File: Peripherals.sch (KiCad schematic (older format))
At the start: 64 parts, among them J10 Conn_01x01, J11 Conn_01x01, J12 Conn_01x01, J13 Conn_01x04, J14 RCAJack, J5 Conn_01x10, J6 Conn_01x10, J7 Conn_01x10, J8 Conn_01x08, J9 Conn_01x01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

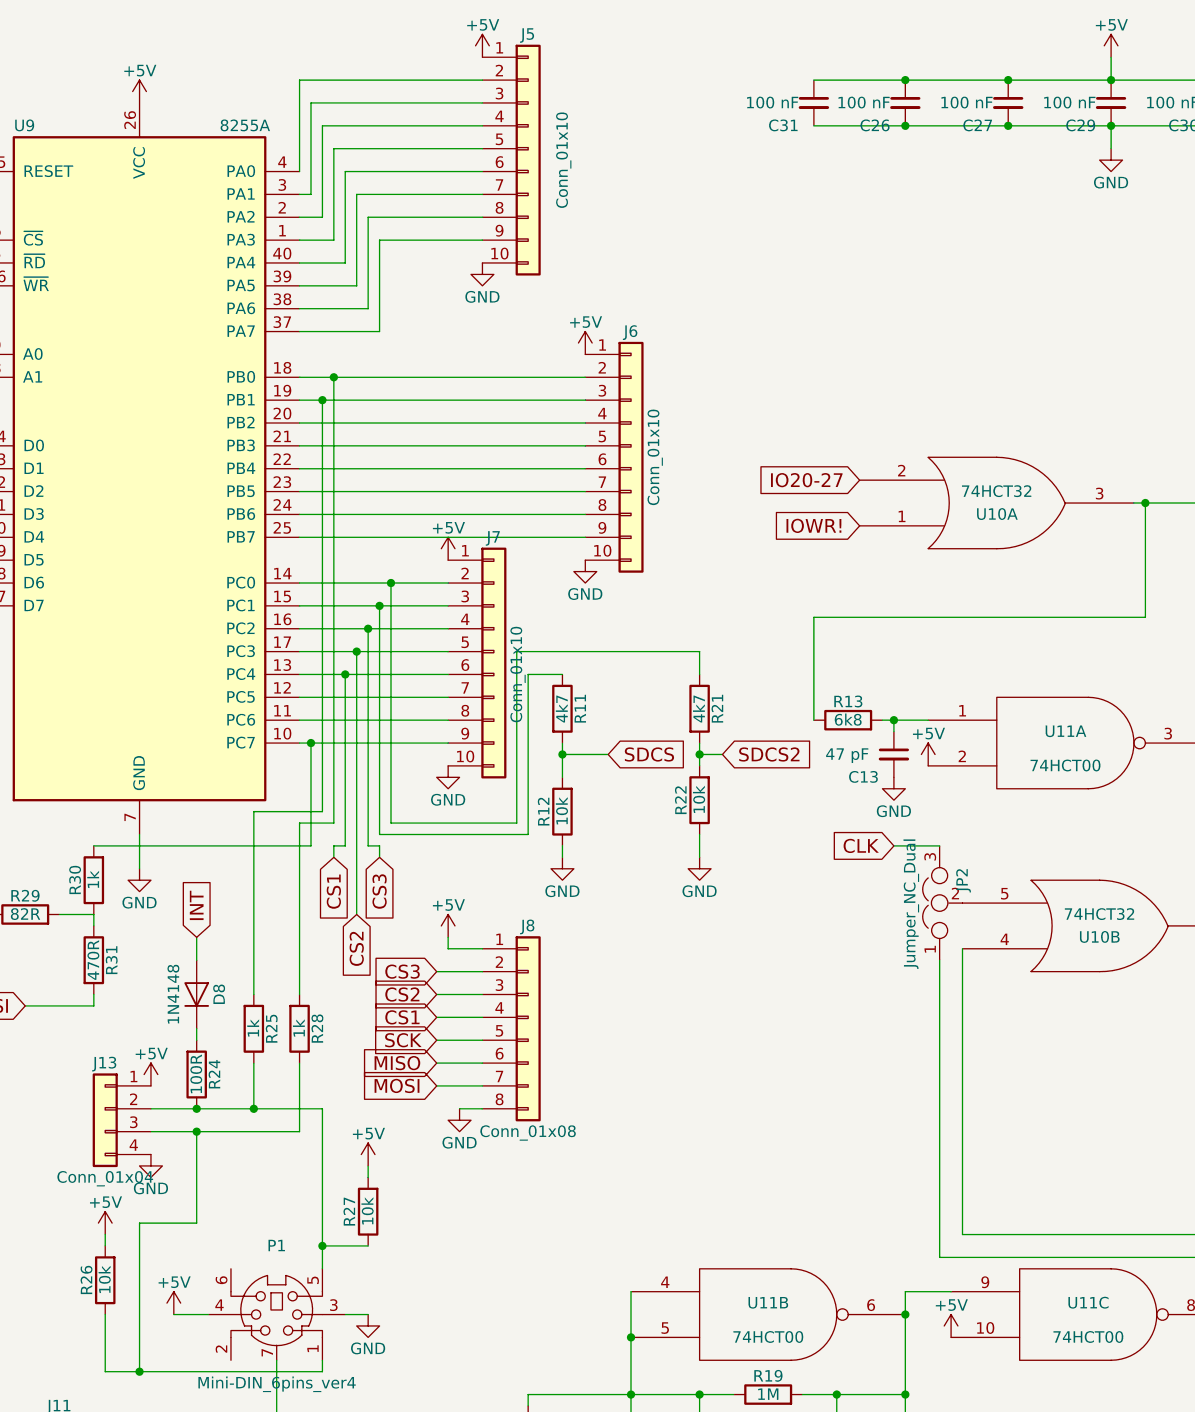
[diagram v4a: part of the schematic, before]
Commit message: Fixed PS/2 interrupt line
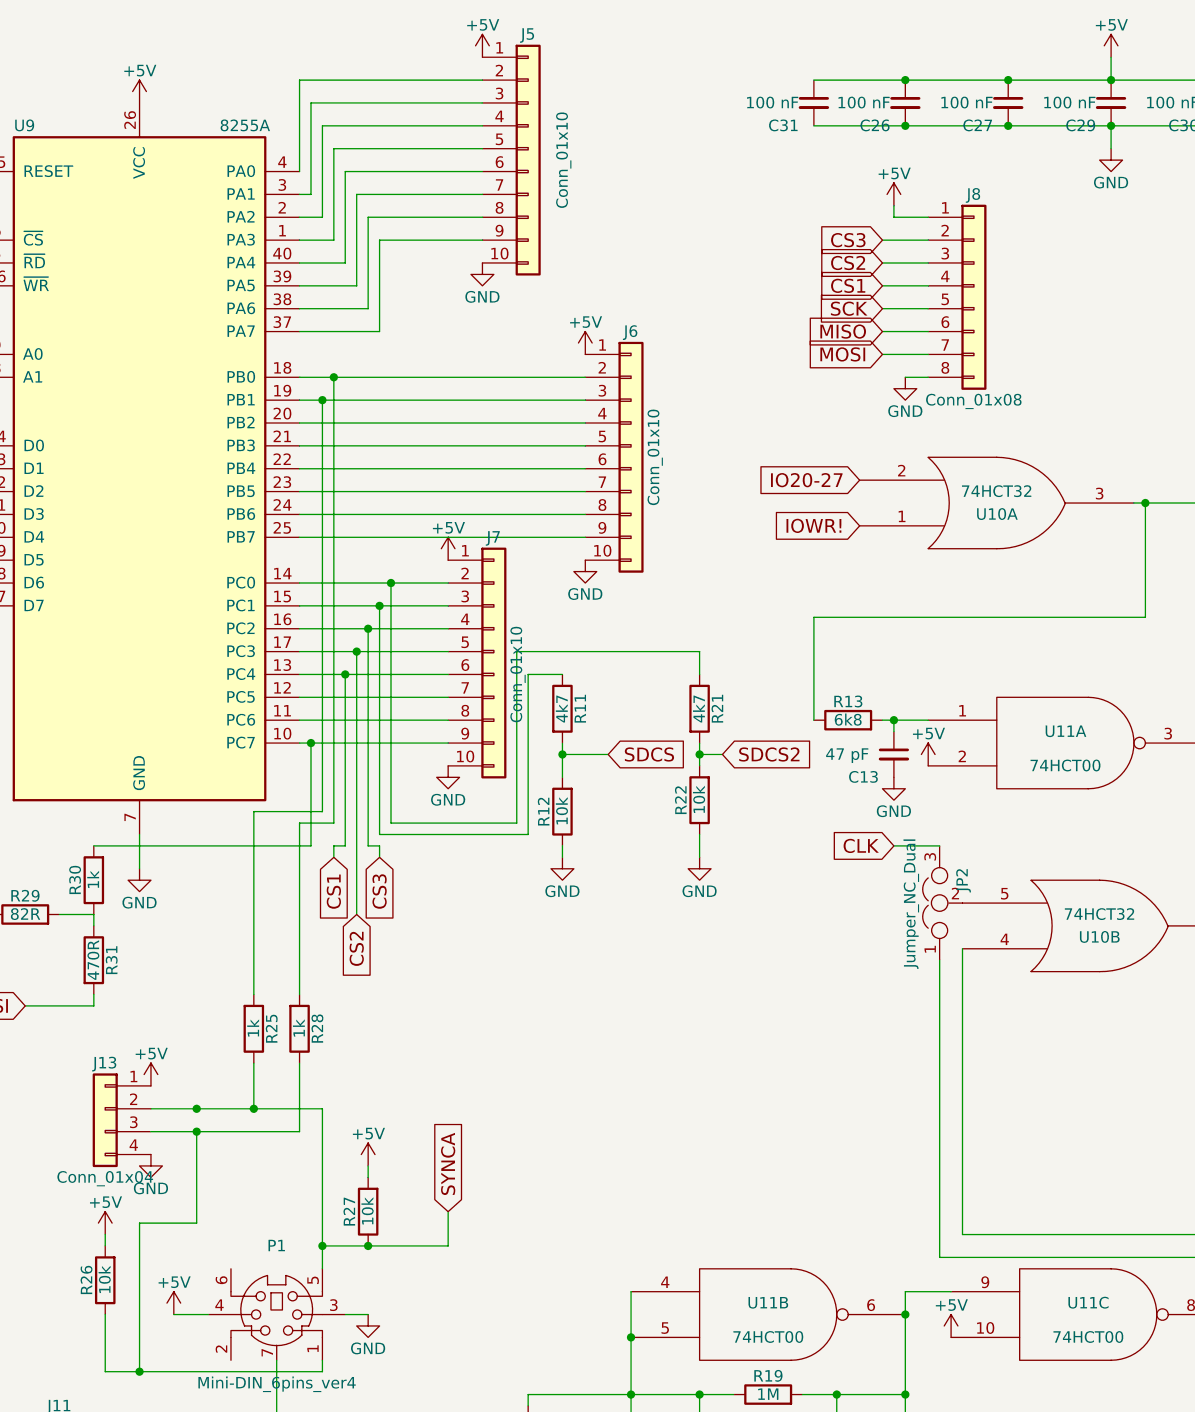
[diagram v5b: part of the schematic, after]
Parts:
- removed D8: 1N4148, Diodes_THT:D_DO-35_SOD27_P7.62mm_Horizontal, symbol D
- removed R24: 100R, Resistors_THT:R_Axial_DIN0207_L6.3mm_D2.5mm_P7.62mm_Horizontal, symbol R
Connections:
- net SYNCA: now reaches J13.2 (Pin_2), P1.5, R25.1, R27.1
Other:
- moved on the sheet: J8

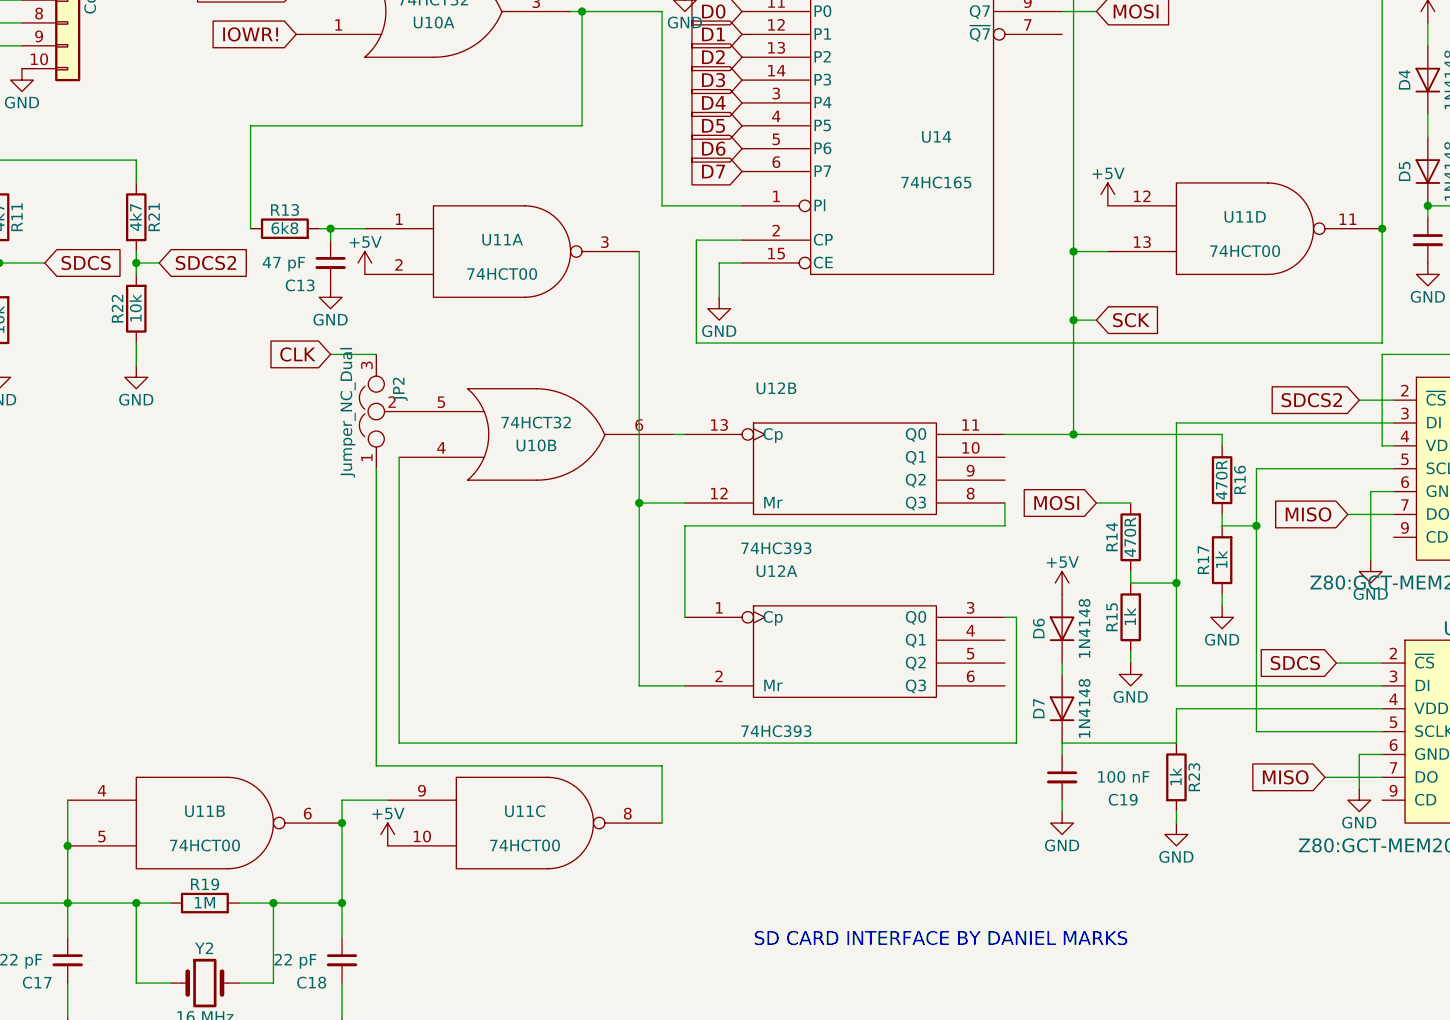
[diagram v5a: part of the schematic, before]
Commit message: Fixed SDHC support, added extra configuration jumpers
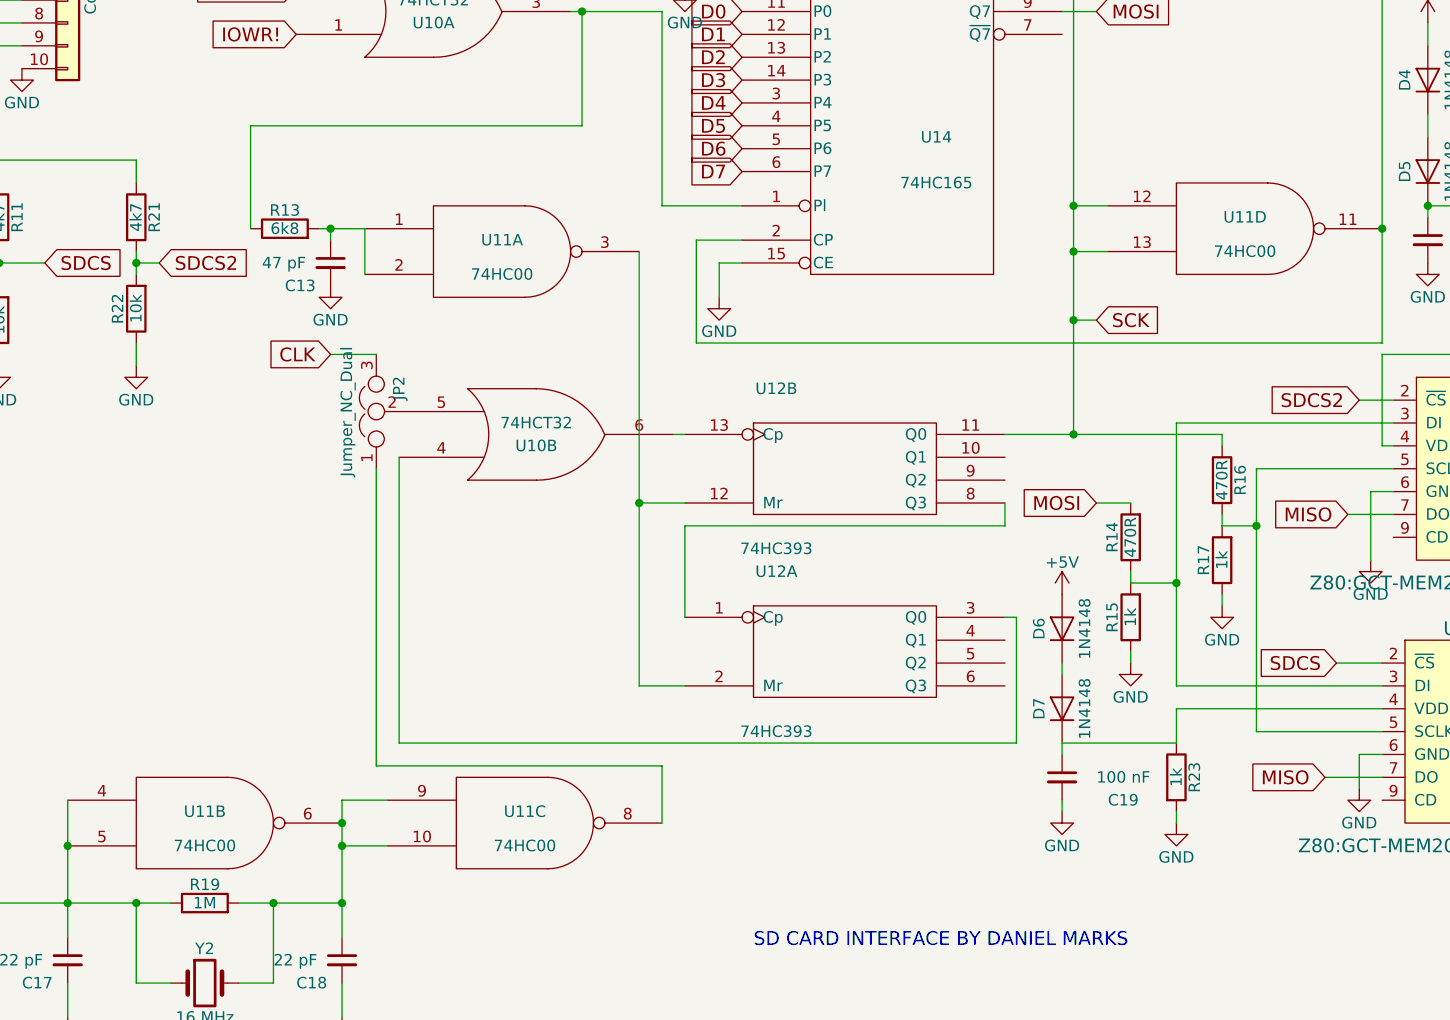
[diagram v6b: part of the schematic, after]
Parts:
- U11: value 74HCT00 -> 74HC00
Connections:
- net +5V: no longer U11.10, U11.12, U11.2
- net SCK: now also U11.12
- net at C13.1, R13.2, U11.1: now also U11.2
- net at C18.1, R19.2, U11.6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: now also U11.10

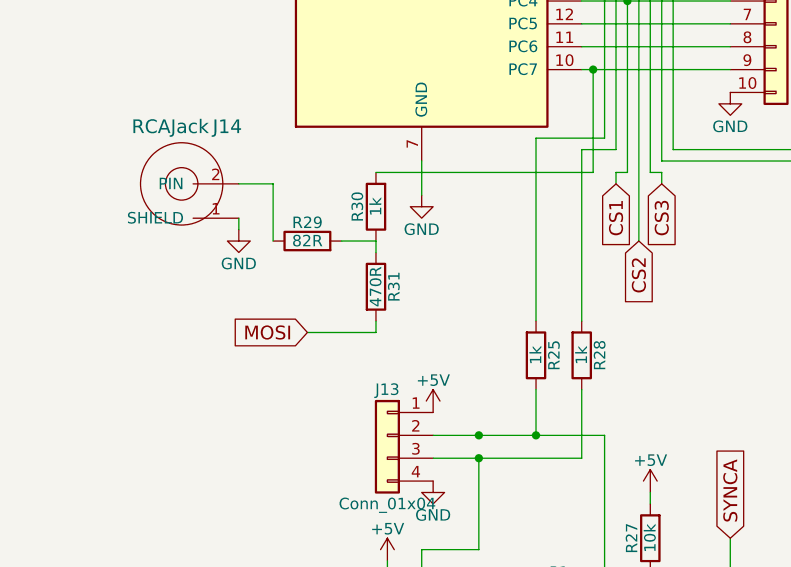
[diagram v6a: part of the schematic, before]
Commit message: Modified video output
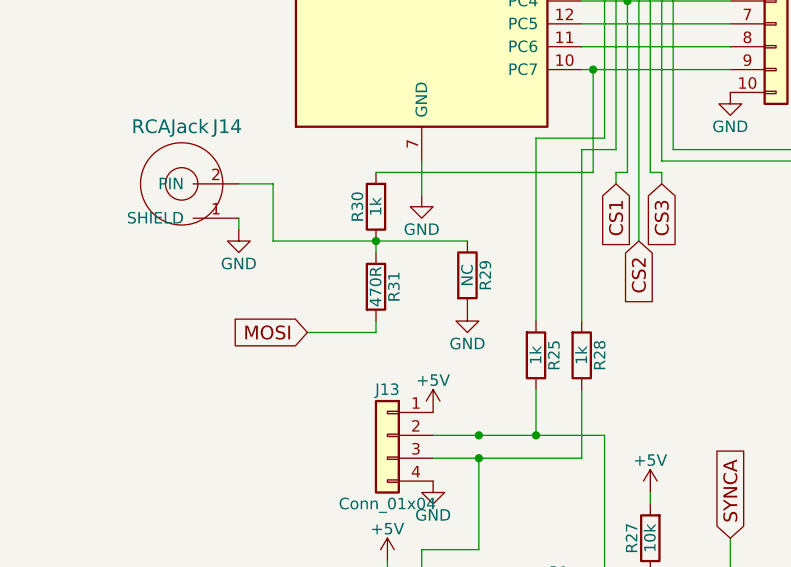
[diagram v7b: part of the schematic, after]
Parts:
- R29: value 82R -> NC
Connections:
- net GND: now also R29.2
- net at R30.1, R31.1: now also J14.2 (PIN), R29.1; no longer R29.2
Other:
- moved on the sheet: R29
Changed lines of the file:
@@
-$EndComp
-$Comp
-L R R29
-U 1 1 608900E5
-P 1750 4550
-F 0 "R29" V 1830 4550 50  0000 C CNN
-F 1 "82R" V 1750 4550 50  0000 C CNN
-F 2 "Resistors_THT:R_Axial_DIN0207_L6.3mm_D2.5mm_P7.62mm_Horizontal" V 1680 4550 50  0001 C CNN
-F 3 "" H 1750 4550 50  0001 C CNN
-	1    1750 4550
-	0    -1   -1   0
 $EndComp
 $Comp
@@
 	2250 4350 2250 4200
 Wire Wire Line
-	1900 4550 2050 4550
+	1600 4550 2450 4550
 Wire Wire Line
 	2050 4550 2050 4600
@@
 Wire Wire Line
 	3900 4150 3900 3400
+$Comp
+L R R29
+U 1 1 608900E5
+P 2450 4700
+F 0 "R29" V 2530 4700 50  0000 C CNN
+F 1 "NC" V 2450 4700 50  0000 C CNN
+F 2 "Resistors_THT:R_Axial_DIN0207_L6.3mm_D2.5mm_P7.62mm_Horizontal" V 2380 4700 50  0001 C CNN
+F 3 "" H 2450 4700 50  0001 C CNN
+	1    2450 4700
+	1    0    0    -1
+$EndComp
+$Comp
+L GND #PWR?
+U 1 1 611C8F01
+P 2450 4850
+F 0 "#PWR?" H 2450 4600 50  0001 C CNN
+F 1 "GND" H 2450 4700 50  0000 C CNN
+F 2 "" H 2450 4850 50  0001 C CNN
+F 3 "" H 2450 4850 50  0001 C CNN
+	1    2450 4850
+	1    0    0    -1
+$EndComp
+Connection ~ 2050 4550
 $EndSCHEMATC
